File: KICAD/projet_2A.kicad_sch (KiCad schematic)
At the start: 3 parts, among them J1 AudioJack3_Ground_Switch

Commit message: alimentation non terminée
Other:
- added sheet alimentation (alimentation.kicad_sch)
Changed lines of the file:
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@@
+	)
+	(sheet
+		(at 39.37 189.23)
+		(size 31.75 33.02)
+		(exclude_from_sim no)
+		(in_bom yes)
+		(on_board yes)
+		(dnp no)
+		(fields_autoplaced yes)
+		(stroke
+			(width 0.1524)
+			(type solid)
+		)
+		(fill
+			(color 0 0 0 0)
+		)
+		(property "Sheetname" "alimentation"
+			(at 39.37 188.5184 0)
+			(show_name no)
+			(do_not_autoplace no)
+			(effects
+				(font
+					(size 1.27 1.27)
+				)
+				(justify left bottom)
+			)
+		)
+		(property "Sheetfile" "alimentation.kicad_sch"
+			(at 39.37 222.8346 0)
+			(show_name no)
+			(do_not_autoplace no)
+			(effects
+				(font
+					(size 1.27 1.27)
+				)
+				(justify left top)
+			)
+		)
+		(instances
+			(project "projet_2A"
+				(path "/05601714-c31e-4eda-914b-0c4b098c219a"
+					(page "7")
+				)
+			)
+		)
 	)
 	(sheet

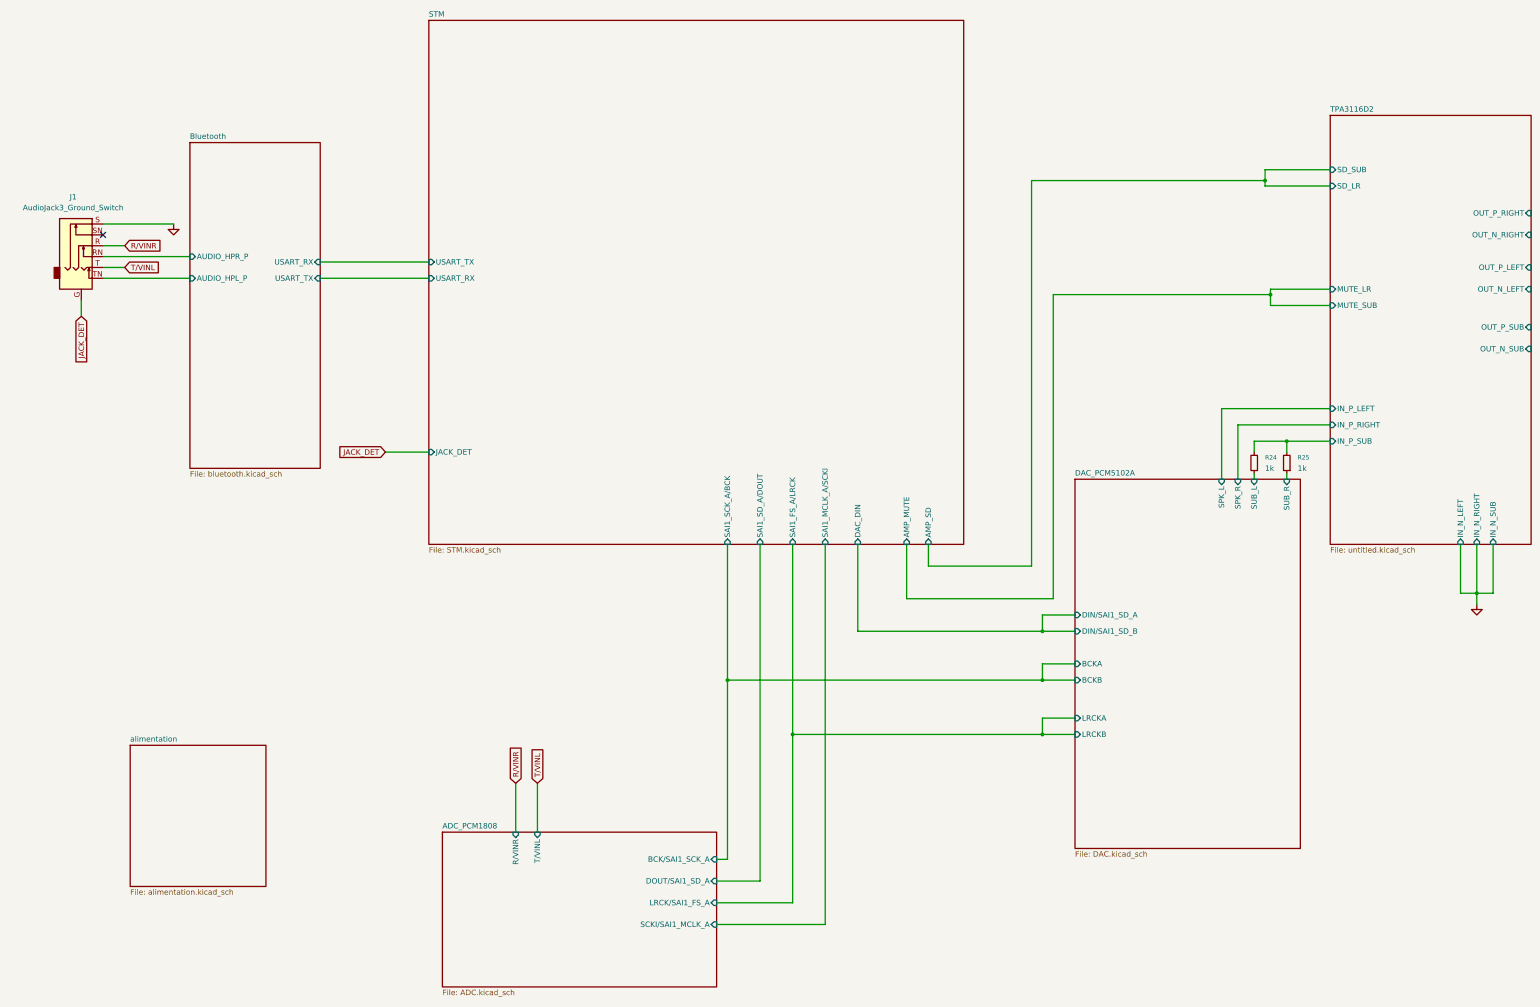
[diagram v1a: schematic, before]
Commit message: supression du subwoofer
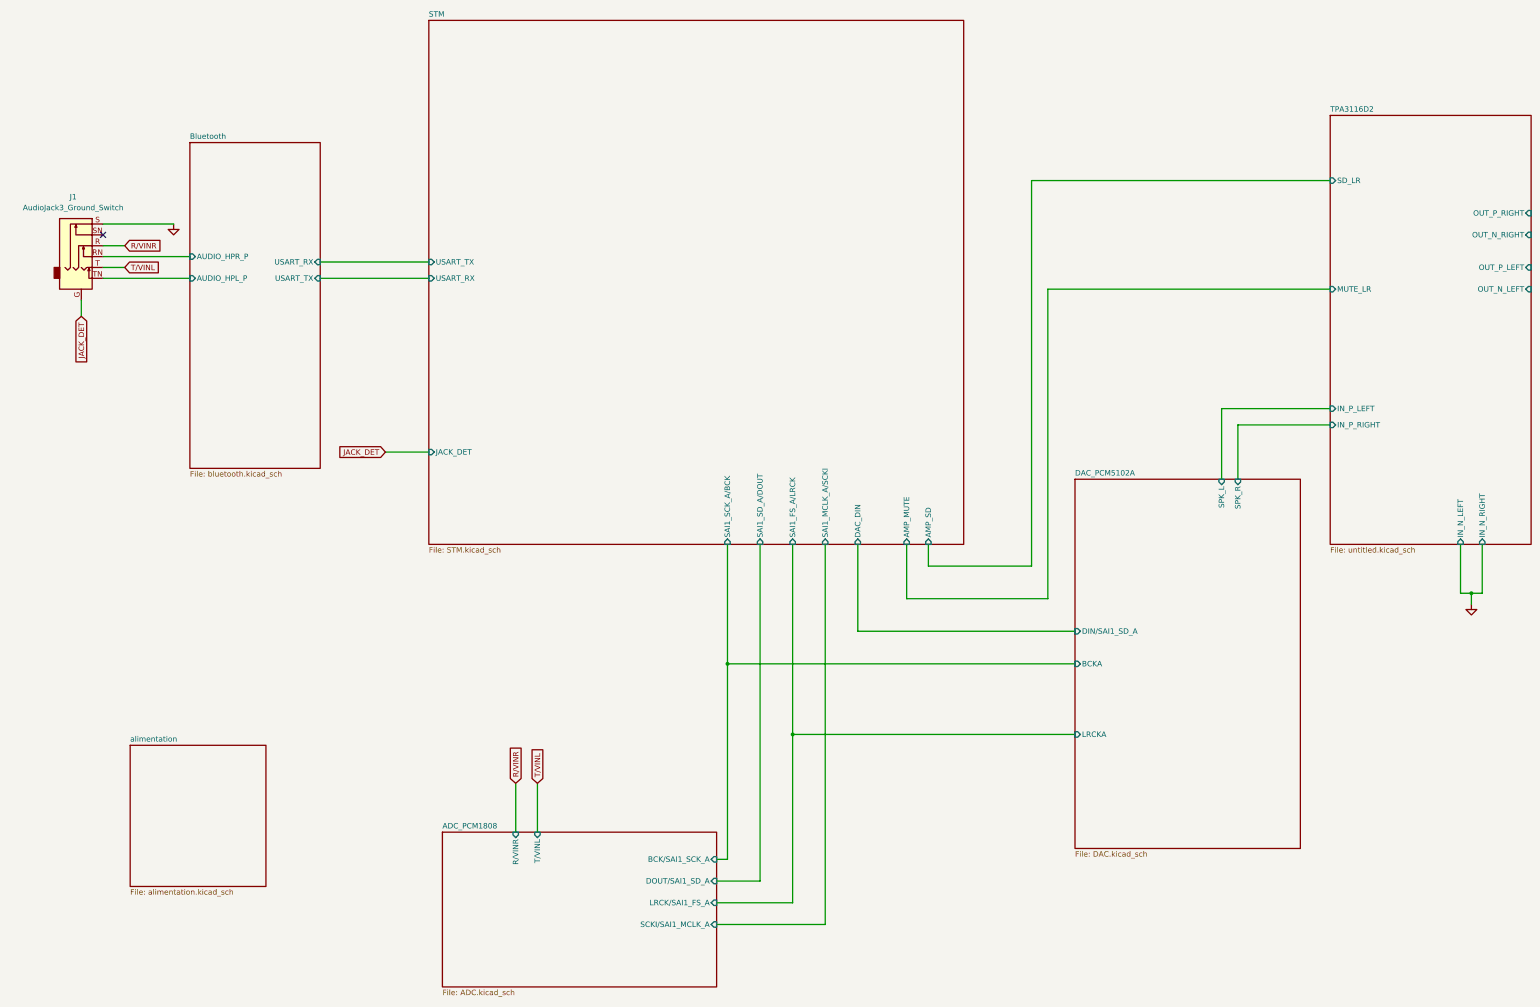
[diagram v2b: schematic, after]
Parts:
- removed R24, R25: 1k, symbol Device:R_Small
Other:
- sheet DAC_PCM5102A ports: added none; removed BCKB, DIN/SAI1_SD_B, LRCKB, SUB_L, SUB_R
- sheet TPA3116D2 ports: added none; removed IN_N_SUB, IN_P_SUB, MUTE_SUB, OUT_N_SUB, OUT_P_SUB, SD_SUB

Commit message: mise en forme globale
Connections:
- net R/VINR renamed JACK_R
- net T/VINL renamed JACK_L
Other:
- sheet ADC_PCM1808 ports: added BCK, DOUT, JACK_L, JACK_R, LRCK, SCKI; removed BCK/SAI1_SCK_A, DOUT/SAI1_SD_A, LRCK/SAI1_FS_A, R/VINR, SCKI/SAI1_MCLK_A, T/VINL
- sheet DAC_PCM5102A ports: added BCK, DIN, LRCK; removed BCKA, DIN/SAI1_SD_A, LRCKA
- sheet STM ports: added BCK, DIN, DOUT, LRCK, SCKI; removed DAC_DIN, SAI1_FS_A/LRCK, SAI1_MCLK_A/SCKI, SAI1_SCK_A/BCK, SAI1_SD_A/DOUT
- sheet TPA3116D2 ports: added AMP_MUTE, AMP_SD, PLIMIT, SPK_L, SPK_R; removed IN_N_LEFT, IN_N_RIGHT, IN_P_LEFT, IN_P_RIGHT, MUTE_LR, SD_LR

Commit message: interface HM
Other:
- added sheet Interface_HM (Interface_HM.kicad_sch)
- sheet ADC_PCM1808 ports: added I2S_BCK, I2S_DOUT, I2S_LRCK, I2S_SCKI; removed BCK, DOUT, LRCK, SCKI
- sheet Bluetooth ports: added BT_RX, BT_TX; removed USART_RX, USART_TX
- sheet DAC_PCM5102A ports: added I2S_BCK, I2S_DIN, I2S_LRCK; removed BCK, DIN, LRCK
- sheet STM ports: added none; removed AMP_MUTE, AMP_SD, BCK, DIN, DOUT, JACK_DET, LRCK, SCKI, USART_RX, USART_TX
- sheet TPA3116D2 ports: added AMP_PLIMIT; removed PLIMIT
- sheet alimentation ports: added USB_ALERT, USB_SCL, USB_SDA; removed none
